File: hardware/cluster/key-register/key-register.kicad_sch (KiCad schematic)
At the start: 2 parts

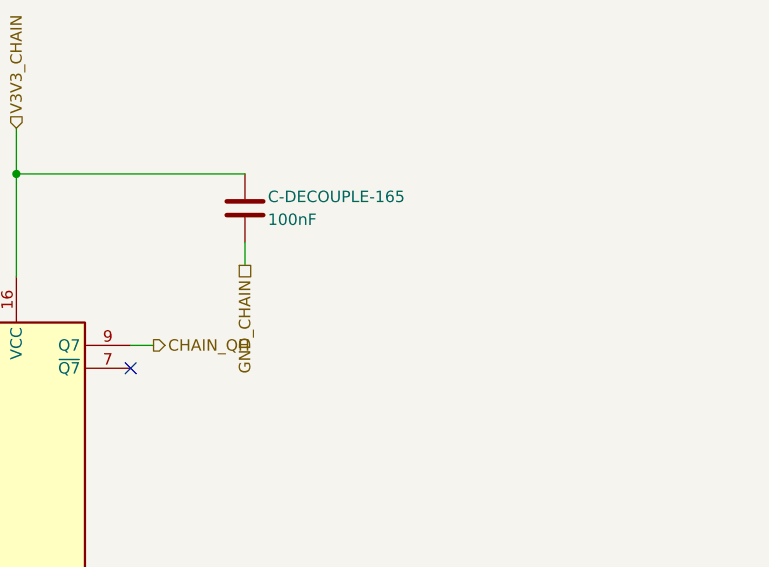
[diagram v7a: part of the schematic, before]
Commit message: Right-hand key board laid out for the Matrix, its J2 escape drawn by hand; U1's second decoupler at VCC (#23, #6-5, #19 F1)
pcb_route cannot fan out J2 (J-MCU-KB) and Freerouting left connections and no pours, so hardware/boards/key-board-rh/matrix_routes.py runs pcb.py layout with J2-J5's nets held out and their routes kept clear, then draws the Matrix's 24 nets: nested 45-degree fans out of both rows, round the header's ends past the tail columns, along the rails on 0.7 mm lanes, each net dropping to its pin through a via. GND_CHAIN pours on both faces with the router's stitching, the connect_first straps by the router as before, J2's front-row grounds and J3.2 tied to the pours. pcb.py check passes; renders and fab/ re-made.

Review #6-5: the key-register sheet gains C-DECOUPLE-165-VCC (C-DECOUPLE-165 qty 8); here it is C9 at U1 pin 16. The left-hand board (C8) and main board (C205, C206) carry it on their sheets and await their layouts. The rails run 0.5 past the Matrix's tail edge for its last pins' edge clearance (body CAD rebuilding). J5 is a 1x4 2.54 mm pin footprint, the wire pads moved below the lanes; setup-env.sh fetches its and the 1x10's 3D models.

Gate-Red: body CAD outputs rebuilding after the rails' end moved; key-board-lh and main-board .kicad_pcb lack the new decoupler until their layouts (wave 3 / re-layout); main-board .kicad_pcb known stale; breath-adc vdd-ripple known
Co-Authored-By: Claude Opus 5.5 <noreply@anthropic.com>
Claude-Session: https://claude.ai/code/session_01LmB4muFXnoLprWX4JzuJ5A
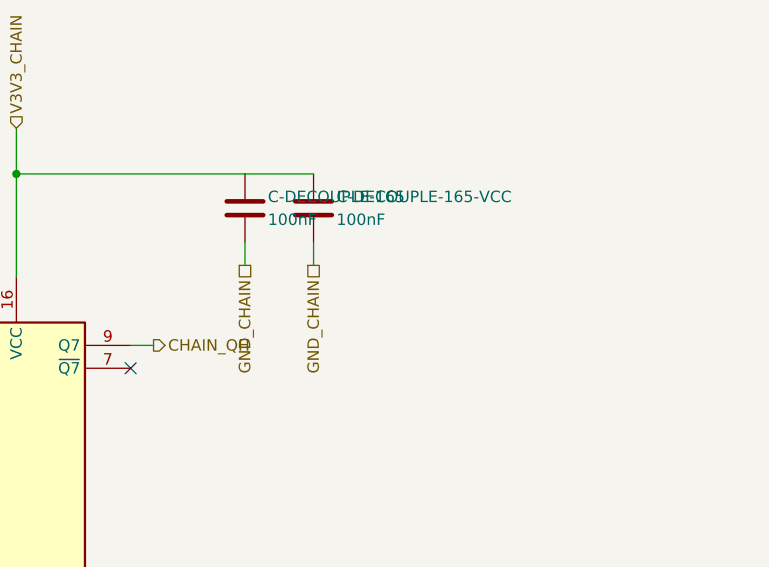
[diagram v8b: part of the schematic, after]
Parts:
- added C-DECOUPLE-165-VCC: 100nF, Capacitor_SMD:C_0805_2012Metric, symbol Device:C
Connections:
- net GND_CHAIN: now also C-DECOUPLE-165-VCC.2
- net V3V3_CHAIN: now also C-DECOUPLE-165-VCC.1
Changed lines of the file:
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@@
     (instances (project "main-board" (path "/b12a49ac-ffa0-5078-b2ba-e15d161f1936/7a50ccf9-a694-5b80-9465-ebb313aea857" (reference "C14") (unit 1))) (project "main-board" (path "/b12a49ac-ffa0-5078-b2ba-e15d161f1936/bb4862a5-79d0-56f6-9d21-4f7ecbf52376" (reference "C13") (unit 1))) (project "key-board-lh" (path "/a2d77fad-366b-59d5-8d08-ccdc7dd94a07/4221457c-e28c-5c2b-bcda-fa08233e468e" (reference "C6") (unit 1))) (project "key-board-rh" (path "/0d798814-7e94-52b0-a143-b50dd4dde890/65d7d4f5-8cbf-508f-a86f-604c3c11ee1c" (reference "C7") (unit 1))) (project "key-register" (path "/1c06c0f3-909c-5b19-ae40-990673d82c30" (reference "C-DECOUPLE-165") (unit 1))))
   )
+  (symbol (lib_id "Device:C") (at 134.62 80.01 0) (unit 1)
+    (in_bom yes) (on_board yes) (dnp no)
+    (property "Reference" "C-DECOUPLE-165-VCC" (at 137.16 78.74 0) (effects (font (size 1.27 1.27)) (justify left)))
+    (property "Value" "100nF" (at 137.16 81.28 0) (effects (font (size 1.27 1.27)) (justify left)))
+    (property "Footprint" "Capacitor_SMD:C_0805_2012Metric" (at 135.89 83.82 0) (effects (font (size 1.27 1.27)) hide))
+    (property "Datasheet" "" (at 134.62 80.01 0) (effects (font (size 1.27 1.27)) hide))
+    (property "Row" "C-DECOUPLE-165" (at 134.62 80.01 0) (effects (font (size 1.27 1.27)) hide))
+    (property "Pins" "1=1 2=2" (at 134.62 80.01 0) (effects (font (size 1.27 1.27)) hide))
+    (property "Note" "The second decoupler, AT VCC (pin 16), its ground straight into the board's ground - review #6-5: the first one's place on a board can leave it far from VCC (the right-hand board's sits beside pin 8, 12 mm from pin 16)" (at 134.62 80.01 0) (effects (font (size 1.27 1.27)) hide))
+    (property "Manufacturer" "YAGEO" (at 134.62 80.01 0) (effects (font (size 1.27 1.27)) hide))
+    (property "MPN" "CC0805KRX7R9BB104" (at 134.62 80.01 0) (effects (font (size 1.27 1.27)) hide))
+    (property "LCSC" "C49678" (at 134.62 80.01 0) (effects (font (size 1.27 1.27)) hide))
+    (property "Assembly" "machine" (at 134.62 80.01 0) (effects (font (size 1.27 1.27)) hide))
+    (pin "1")
+    (pin "2")
+    (instances (project "main-board" (path "/b12a49ac-ffa0-5078-b2ba-e15d161f1936/7a50ccf9-a694-5b80-9465-ebb313aea857" (reference "C205") (unit 1))) (project "main-board" (path "/b12a49ac-ffa0-5078-b2ba-e15d161f1936/bb4862a5-79d0-56f6-9d21-4f7ecbf52376" (reference "C206") (unit 1))) (project "key-board-lh" (path "/a2d77fad-366b-59d5-8d08-ccdc7dd94a07/4221457c-e28c-5c2b-bcda-fa08233e468e" (reference "C8") (unit 1))) (project "key-board-rh" (path "/0d798814-7e94-52b0-a143-b50dd4dde890/65d7d4f5-8cbf-508f-a86f-604c3c11ee1c" (reference "C9") (unit 1))) (project "key-register" (path "/1c06c0f3-909c-5b19-ae40-990673d82c30" (reference "C-DECOUPLE-165-VCC") (unit 1))))
+  )
+  (wire (pts (xy 127.0 76.2) (xy 134.62 76.2)) (stroke (width 0) (type default)))
+  (wire (pts (xy 134.62 83.82) (xy 134.62 86.36)) (stroke (width 0) (type default)))
+  (hierarchical_label "GND_CHAIN" (shape passive) (at 134.62 86.36 270) (effects (font (size 1.27 1.27)) (justify right))
+    (property "Dir" "ref" (at 134.62 86.36 0) (effects (font (size 1.27 1.27)) hide))
+    (property "From" "interfaces/key-chain-loom" (at 134.62 86.36 0) (effects (font (size 1.27 1.27)) hide))
+    (property "Figure" "chain-conductors" (at 134.62 86.36 0) (effects (font (size 1.27 1.27)) hide)))
   (wire (pts (xy 101.6 87.63) (xy 101.6 76.2)) (stroke (width 0) (type default)))
   (wire (pts (xy 101.6 76.2) (xy 127.0 76.2)) (stroke (width 0) (type default)))
